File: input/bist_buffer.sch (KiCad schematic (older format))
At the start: 7 parts, among them U9 OPA1679

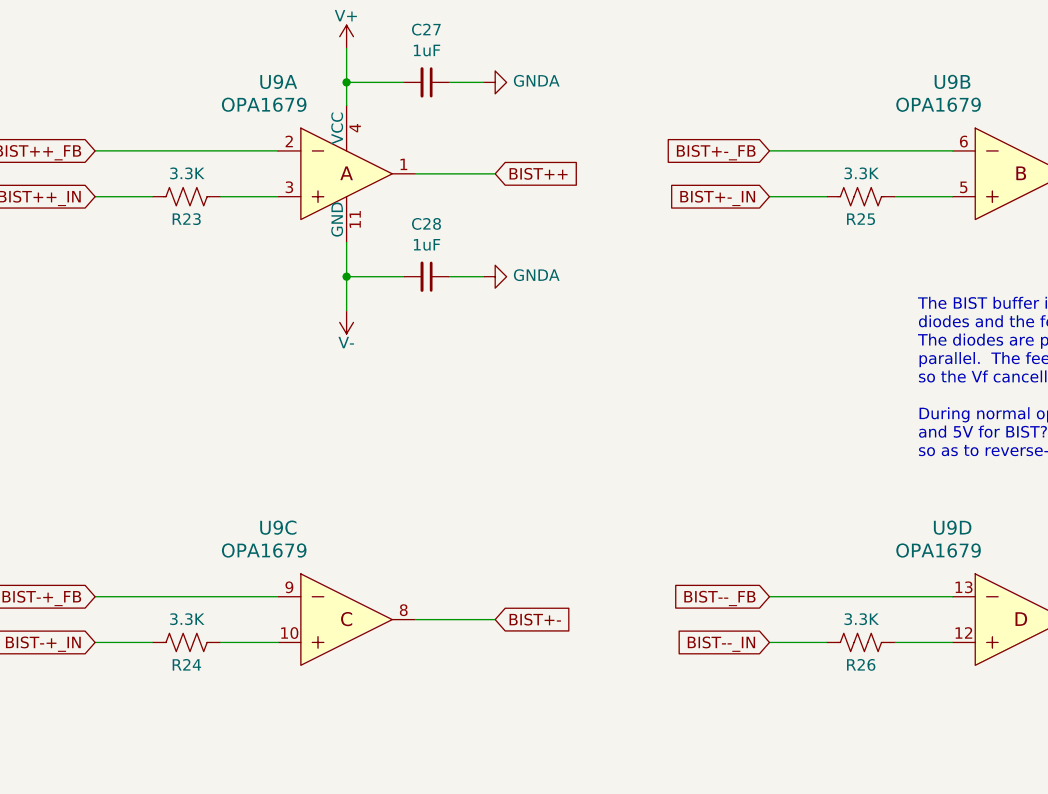
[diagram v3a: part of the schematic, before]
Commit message: Checkpoint before starting routing.  Added power and ground testpoints.
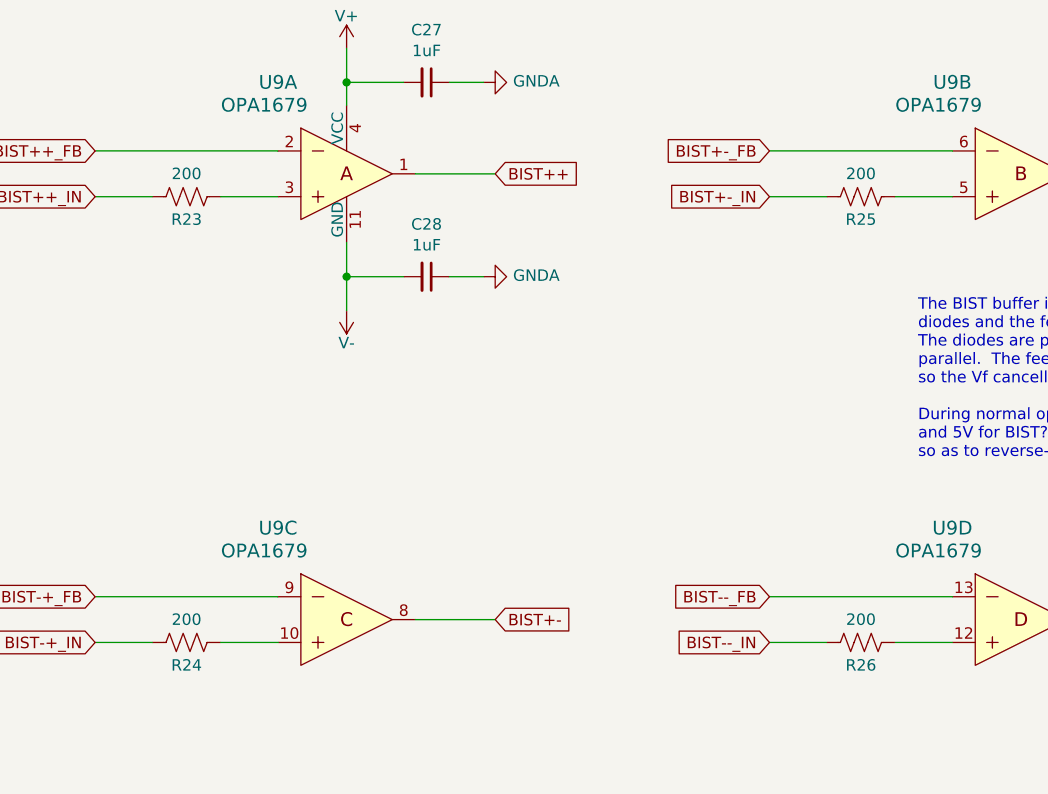
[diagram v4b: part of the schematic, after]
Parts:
- C27, C28: DK line (none) -> 27
- R23, R24, R25, R26: value 3.3K -> 200; DK line (none) -> 55; Description (none) -> 200 Ohms ±1% 0.125W, 1/8W Chip Resistor 0603 (1608 Metric) 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; Digikey (none) -> RNCP0603FTD200RCT-ND; Notes 0.1% -> (none)
- U9: DK line (none) -> 31; Description IC AUDIO 4 CIRCUIT 14SOIC -> (none)
- U9: DK line (none) -> 31; Description IC OPAMP GP 4 CIRCUIT 14SOIC -> (none)
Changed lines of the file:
@@
 EESchema Schematic File Version 4
-LIBS:input_board-cache
-EELAYER 29 0
+EELAYER 30 0
 EELAYER END
 $Descr A4 11693 8268
@@
 F 3 "http://www.ti.com/general/docs/suppproductinfo.tsp?distId=10&gotoUrl=http%3A%2F%2Fwww.ti.com%2Flit%2Fgpn%2Fopa1679" H 5100 3400 60  0001 L CNN
 F 4 "OPA1679IDR" H 5100 3600 60  0001 L CNN "MPN"
-F 5 "IC AUDIO 4 CIRCUIT 14SOIC" H 5100 4100 60  0001 L CNN "Description"
+F 5 "" H 5100 4100 60  0001 L CNN "Description"
 F 6 "Texas Instruments" H 5100 4200 60  0001 L CNN "Manufacturer"
 F 7 "296-46621-1-ND" H 4900 3100 50  0001 C CNN "Digikey"
+F 8 "31" H 4900 3100 50  0001 C CNN "DK line"
 	1    4900 3100
 	1    0    0    -1
@@
 F 5 "1276-6471-1-ND" H 5250 2700 50  0001 C CNN "Digikey"
 F 6 "CL21B105KOFNNNG" H 5250 2700 50  0001 C CNN "MPN"
+F 7 "27" H 5250 2700 50  0001 C CNN "DK line"
 	1    5250 2700
 	0    1    1    0
@@
 F 5 "1276-6471-1-ND" H 5250 3550 50  0001 C CNN "Digikey"
 F 6 "CL21B105KOFNNNG" H 5250 3550 50  0001 C CNN "MPN"
+F 7 "27" H 5250 3550 50  0001 C CNN "DK line"
 	1    5250 3550
 	0    1    1    0
@@
 AR Path="/5E5A51EB/5E5B741A" Ref="R23"  Part="1"
 F 0 "R23" V 4300 3200 50  0000 C CNN
-F 1 "3.3K" V 4100 3200 50  0000 C CNN
+F 1 "200" V 4100 3200 50  0000 C CNN
 F 2 "Resistor_SMD:R_0603_1608Metric" V 4240 3190 50  0001 C CNN
 F 3 "~" H 4200 3200 50  0001 C CNN
-F 4 "0.1%" H 4200 3200 50  0001 C CNN "Notes"
+F 4 "" H 4200 3200 50  0001 C CNN "Notes"
+F 5 "55" H 4200 3200 50  0001 C CNN "DK line"
+F 6 "200 Ohms ±1% 0.125W, 1/8W Chip Resistor 0603 (1608 Metric) Anti-Sulfur, Moisture Resistant Thin Film" H 4200 3200 50  0001 C CNN "Description"
+F 7 "RNCP0603FTD200RCT-ND" H 4200 3200 50  0001 C CNN "Digikey"
 	1    4200 3200
 	0    1    1    0
@@
 F 3 "http://www.ti.com/general/docs/suppproductinfo.tsp?distId=10&gotoUrl=http%3A%2F%2Fwww.ti.com%2Flit%2Fgpn%2Fopa1679" H 8050 3400 60  0001 L CNN
 F 4 "LM324ADR" H 8050 3600 60  0001 L CNN "MPN"
-F 5 "IC OPAMP GP 4 CIRCUIT 14SOIC" H 8050 4100 60  0001 L CNN "Description"
+F 5 "" H 8050 4100 60  0001 L CNN "Description"
 F 6 "Texas Instruments" H 8050 4200 60  0001 L CNN "Manufacturer"
 F 7 "296-46621-1-ND" H 7850 3100 50  0001 C CNN "Digikey"
@@
 F 12 "Linear - Amplifiers - Instrumentation, OP Amps, Buffer Amps" H 7850 3100 50  0001 C CNN "Family"
 F 13 "Active" H 7850 3100 50  0001 C CNN "Status"
+F 14 "31" H 7850 3100 50  0001 C CNN "DK line"
 	2    7850 3100
 	1    0    0    -1
@@
 AR Path="/5E5A51EB/5E5BA20D" Ref="R25"  Part="1"
 F 0 "R25" V 7250 3200 50  0000 C CNN
-F 1 "3.3K" V 7050 3200 50  0000 C CNN
+F 1 "200" V 7050 3200 50  0000 C CNN
 F 2 "Resistor_SMD:R_0603_1608Metric" V 7190 3190 50  0001 C CNN
 F 3 "~" H 7150 3200 50  0001 C CNN
-F 4 "0.1%" H 7150 3200 50  0001 C CNN "Notes"
+F 4 "" H 7150 3200 50  0001 C CNN "Notes"
+F 5 "55" H 7150 3200 50  0001 C CNN "DK line"
+F 6 "200 Ohms ±1% 0.125W, 1/8W Chip Resistor 0603 (1608 Metric) Anti-Sulfur, Moisture Resistant Thin Film" H 7150 3200 50  0001 C CNN "Description"
+F 7 "RNCP0603FTD200RCT-ND" H 7150 3200 50  0001 C CNN "Digikey"
 	1    7150 3200
 	0    1    1    0
@@
 F 3 "http://www.ti.com/general/docs/suppproductinfo.tsp?distId=10&gotoUrl=http%3A%2F%2Fwww.ti.com%2Flit%2Fgpn%2Fopa1679" H 5100 5350 60  0001 L CNN
 F 4 "LM324ADR" H 5100 5550 60  0001 L CNN "MPN"
-F 5 "IC OPAMP GP 4 CIRCUIT 14SOIC" H 5100 6050 60  0001 L CNN "Description"
+F 5 "" H 5100 6050 60  0001 L CNN "Description"
 F 6 "Texas Instruments" H 5100 6150 60  0001 L CNN "Manufacturer"
 F 7 "296-46621-1-ND" H 4900 5050 50  0001 C CNN "Digikey"
@@
 F 12 "Linear - Amplifiers - Instrumentation, OP Amps, Buffer Amps" H 4900 5050 50  0001 C CNN "Family"
 F 13 "Active" H 4900 5050 50  0001 C CNN "Status"
+F 14 "31" H 4900 5050 50  0001 C CNN "DK line"
 	3    4900 5050
 	1    0    0    -1
@@
 AR Path="/5E5A51EB/5E5CB3B9" Ref="R24"  Part="1"
 F 0 "R24" V 4300 5150 50  0000 C CNN
-F 1 "3.3K" V 4100 5150 50  0000 C CNN
+F 1 "200" V 4100 5150 50  0000 C CNN
 F 2 "Resistor_SMD:R_0603_1608Metric" V 4240 5140 50  0001 C CNN
 F 3 "~" H 4200 5150 50  0001 C CNN
-F 4 "0.1%" H 4200 5150 50  0001 C CNN "Notes"
+F 4 "" H 4200 5150 50  0001 C CNN "Notes"
+F 5 "55" H 4200 5150 50  0001 C CNN "DK line"
+F 6 "200 Ohms ±1% 0.125W, 1/8W Chip Resistor 0603 (1608 Metric) Anti-Sulfur, Moisture Resistant Thin Film" H 4200 5150 50  0001 C CNN "Description"
+F 7 "RNCP0603FTD200RCT-ND" H 4200 5150 50  0001 C CNN "Digikey"
 	1    4200 5150
 	0    1    1    0
@@
 F 3 "http://www.ti.com/general/docs/suppproductinfo.tsp?distId=10&gotoUrl=http%3A%2F%2Fwww.ti.com%2Flit%2Fgpn%2Fopa1679" H 8050 5350 60  0001 L CNN
 F 4 "OPA1679IDR" H 8050 5550 60  0001 L CNN "MPN"
-F 5 "IC AUDIO 4 CIRCUIT 14SOIC" H 8050 6050 60  0001 L CNN "Description"
+F 5 "" H 8050 6050 60  0001 L CNN "Description"
 F 6 "Texas Instruments" H 8050 6150 60  0001 L CNN "Manufacturer"
 F 7 "296-46621-1-ND" H 7850 5050 50  0001 C CNN "Digikey"
+F 8 "31" H 7850 5050 50  0001 C CNN "DK line"
 	4    7850 5050
 	1    0    0    -1
@@
 AR Path="/5E5A51EB/5E5CB3D1" Ref="R26"  Part="1"
 F 0 "R26" V 7250 5150 50  0000 C CNN
-F 1 "3.3K" V 7050 5150 50  0000 C CNN
+F 1 "200" V 7050 5150 50  0000 C CNN
 F 2 "Resistor_SMD:R_0603_1608Metric" V 7190 5140 50  0001 C CNN
 F 3 "~" H 7150 5150 50  0001 C CNN
-F 4 "0.1%" H 7150 5150 50  0001 C CNN "Notes"
+F 4 "" H 7150 5150 50  0001 C CNN "Notes"
+F 5 "55" H 7150 5150 50  0001 C CNN "DK line"
+F 6 "200 Ohms ±1% 0.125W, 1/8W Chip Resistor 0603 (1608 Metric) Anti-Sulfur, Moisture Resistant Thin Film" H 7150 5150 50  0001 C CNN "Description"
+F 7 "RNCP0603FTD200RCT-ND" H 7150 5150 50  0001 C CNN "Digikey"
 	1    7150 5150
 	0    1    1    0

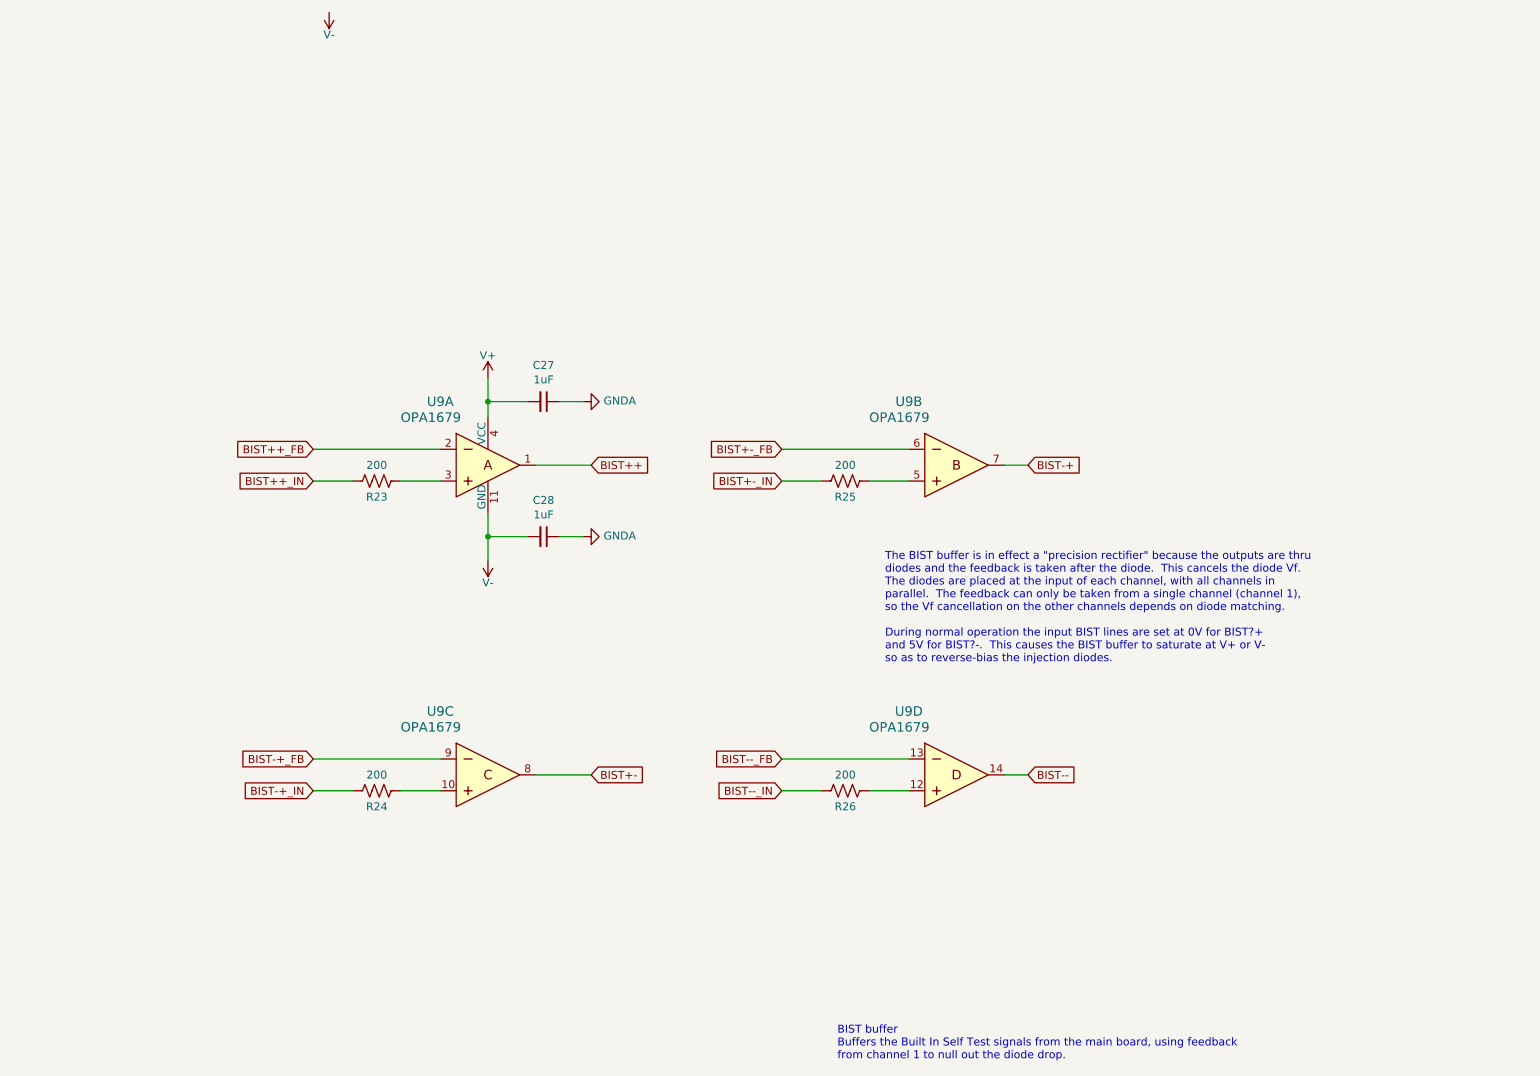
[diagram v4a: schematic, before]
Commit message: Minor tweaks to schematic, and ongoing progress on PCB layout.
Changed BIST buffer to run off of CHAN1_V+, not the global V+.  This caused the CHAN_V+ net name to change.
On power.sch, added bypass caps for the VREF inputs to the V+/V- regulators.  Also, the BIST input lines now
have an RC filter, not just a resistor.
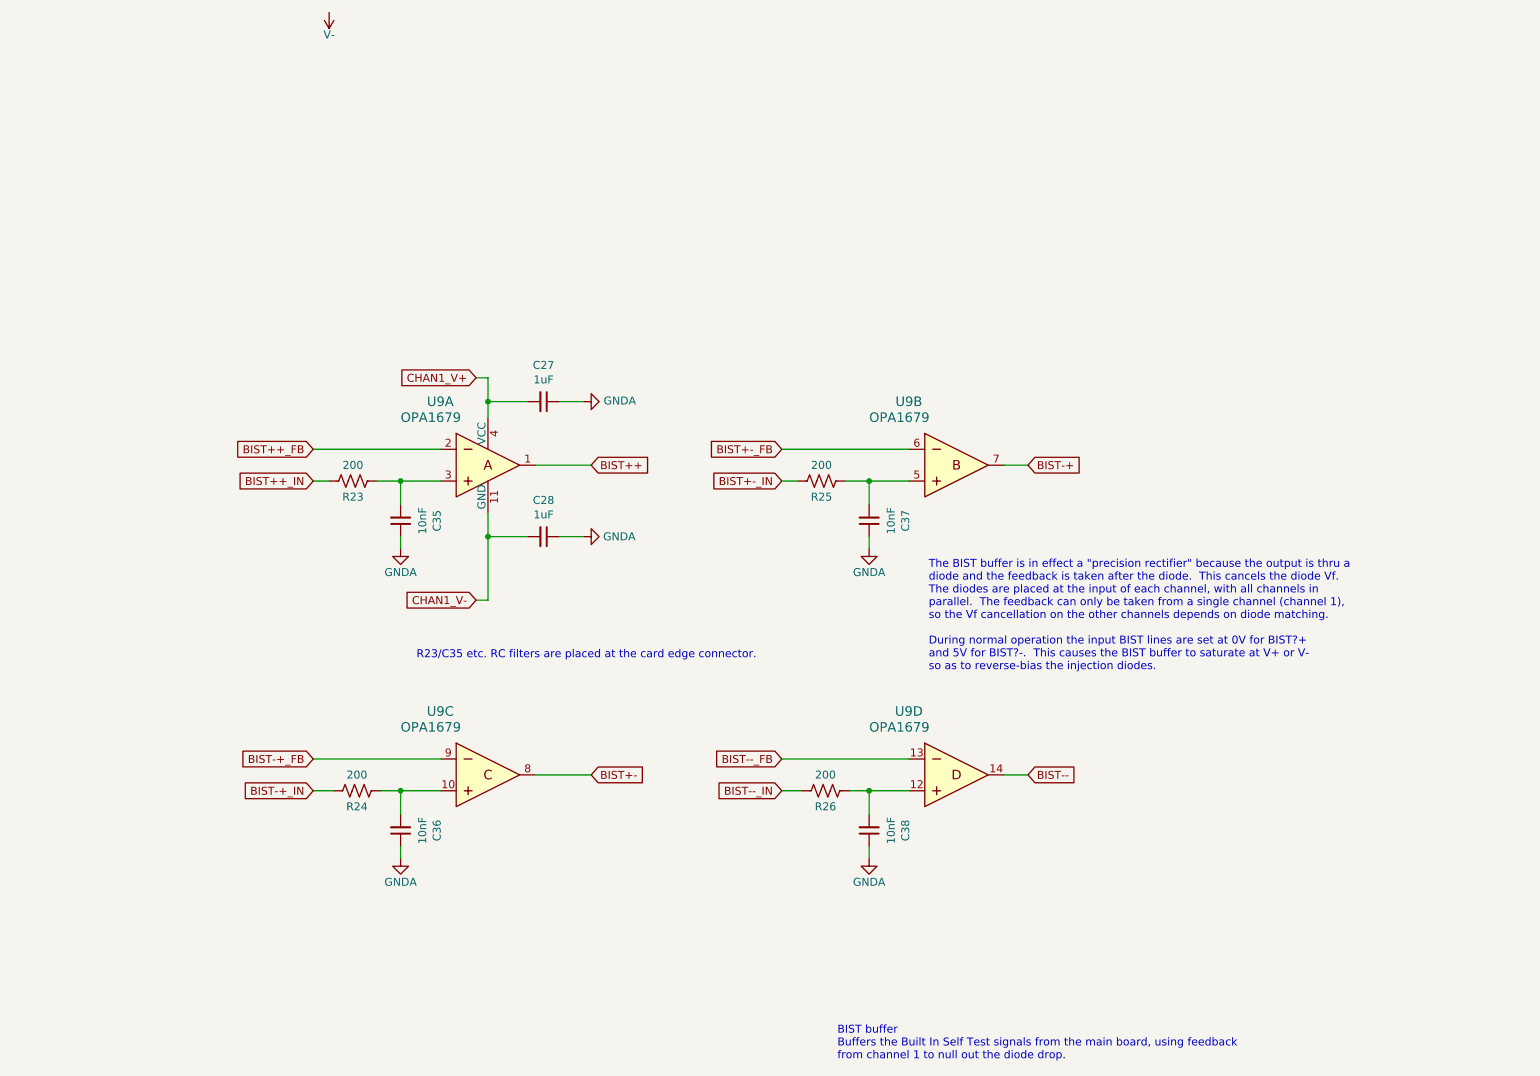
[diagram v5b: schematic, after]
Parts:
- added C35, C36, C37, C38: 10nF, Capacitor_SMD:C_0805_2012Metric, symbol Device:C_Small
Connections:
- net GNDA: now also C35.1, C36.1, C37.1, C38.1
- net V-: no longer C28.2, U9.11 (GND)
- net at R23.1, U9.3: now also C35.2
- net at R25.1, U9.5: now also C37.2
- net at R24.1, U9.10: now also C36.2
- net at R26.1, U9.12: now also C38.2
- net V+ renamed CHAN1_V+
- new net CHAN1_V-: C28.2, U9.11 (GND)
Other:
- note added: "R23/C35 etc. RC filters are placed at the card edge connector."
- note added: "The BIST buffer is in effect a "precision rectifier" because the output is thru a\ndiode and the feedback is taken after the diode. This cancels the diode Vf.\nThe diodes are placed at the input of each channel, with all channels in \nparallel. The feedback can only be taken from a single channel (channel 1),\nso the Vf cancellation on the other channels depends on diode matching.\n\nDuring norma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"
- note removed: "The BIST buffer is in effect a "precision rectifier" because the outputs are thru\ndiodes and the feedback is taken after the diode. This cancels the diode Vf.\nThe diodes are placed at the input of each channel, with all channels in \nparallel. The feedback can only be taken from a single channel (channel 1),\nso the Vf cancellation on the other channels depends on diode matching.\n\nDuring norm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"
- moved on the sheet: R23, R24, R25, R26

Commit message: Various tweaks to schematic which help in the PCB view, mainly getting informative net names. Also unscrambled the + and - paths in the input channel.  This avoided a cross-over before the first stage, and an unintended inversion, but mostly just made net naming less confusing.
Getting better net names made it easier to review the PCB to see if it made sense.  I checked
the ICs on the PCB against the datasheet pinout, and while doing this fixed an actual bug where
I had BIST-+ and BIST+-swapped.

I made some tweaks on the PCB to try to equalize the copper area on the input nets so as to
match the capacitance.  I tweaked the top-side ground pours somewhat, adding in the regulator
area, removing around the high speed traces.

Some changes from gerber viewing.  I reduced the solder mask clearances so that we get mask
web between the SOIC and DFN pads.  I reduced the pad size of the big via from 1.2 to 1.0 mm.
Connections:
- net BIST+-: now also U9.7; no longer U9.8
- net BIST-+: now also U9.8; no longer U9.7
- net U9A+: now reaches C35.2, R23.1, U9.3
- net U9B+: now reaches C37.2, R25.1, U9.5
- net U9C+: now reaches C36.2, R24.1, U9.10
- net U9D+: now reaches C38.2, R26.1, U9.12
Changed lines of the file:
@@
 Connection ~ 4900 3550
 Text GLabel 8300 3100 2    50   Input ~ 0
-BIST-+
+BIST+-
 Text GLabel 8300 5050 2    50   Input ~ 0
 BIST--
@@
 BIST++
 Text GLabel 5550 5050 2    50   Input ~ 0
-BIST+-
+BIST-+
 Text GLabel 3800 5150 0    50   Input ~ 0
 BIST-+_IN
@@
 Wire Wire Line
 	4900 3550 4900 3950
+Text Label 4400 3200 0    50   ~ 0
+U9A+
+Text Label 7350 3200 0    50   ~ 0
+U9B+
+Text Label 4400 5150 0    50   ~ 0
+U9C+
+Text Label 7350 5150 0    50   ~ 0
+U9D+
 $EndSCHEMATC
